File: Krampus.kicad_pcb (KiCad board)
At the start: 2 copper layers, 30 parts, among them J1 AVR-ISP-6, Q1 Q_NMOS_GSD, Q2 Q_NMOS_GSD, SW1 SW_SPDT_Flipped, SW2 SW_SPDT, U1 ATtiny4-TS-PROG

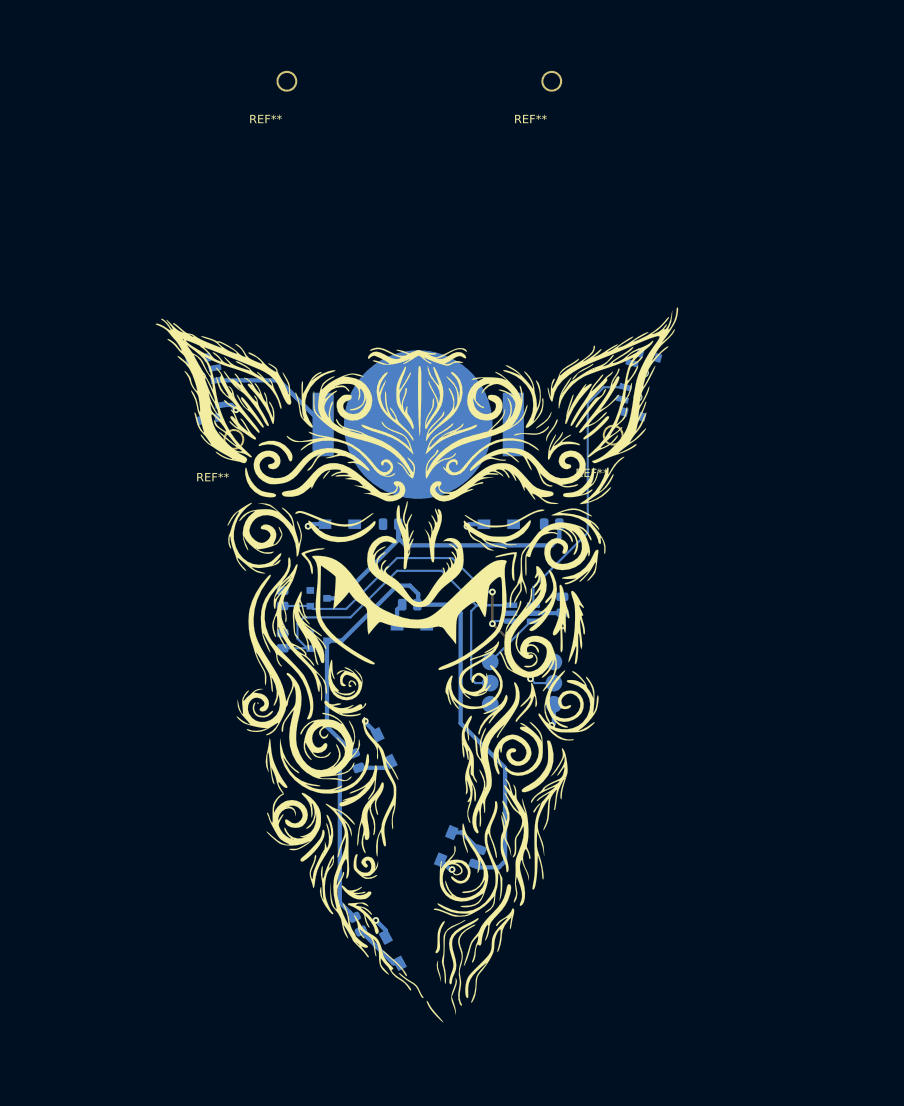
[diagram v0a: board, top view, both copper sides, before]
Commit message: Added copper pours and keepout areas for tongue and eyes. Everything done except edge cuts and revised mouth (want it to be gold)
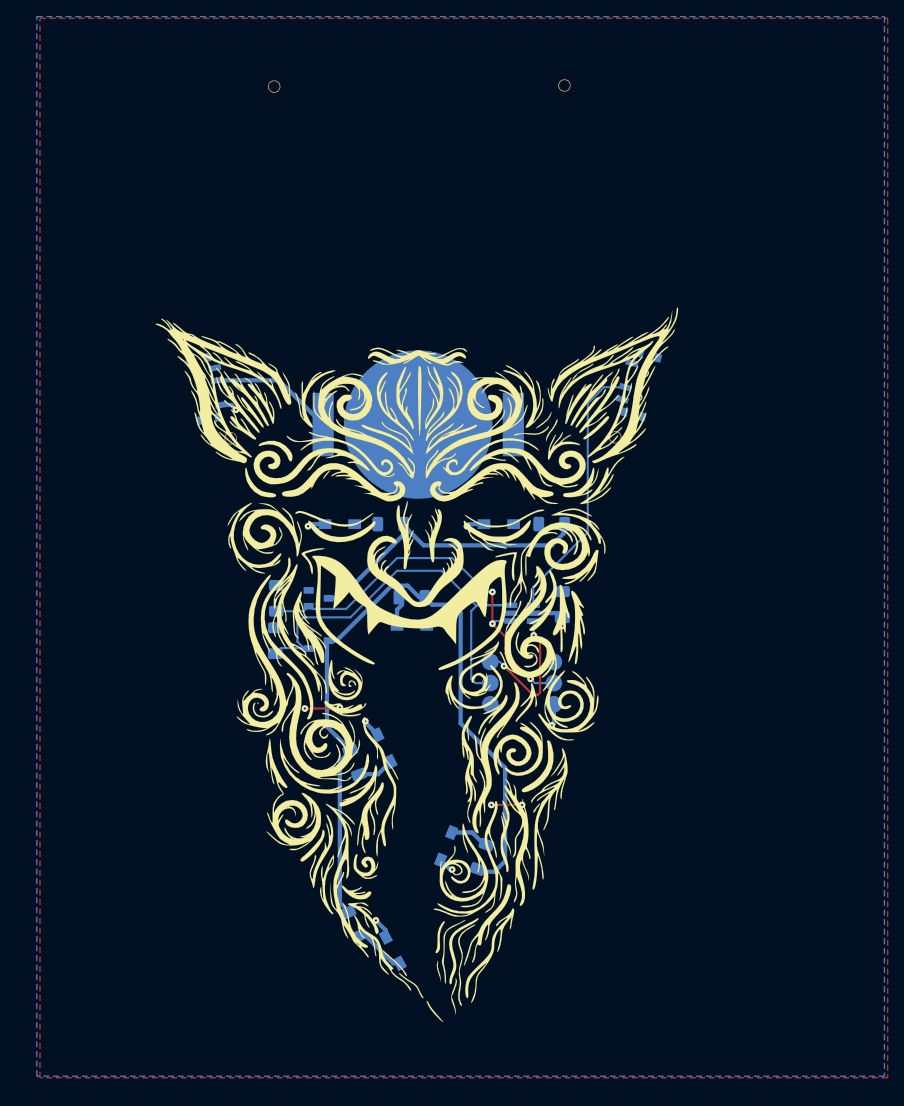
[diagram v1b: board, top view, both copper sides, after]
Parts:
- removed the REF** at (46.5, 80.8)
- removed the REF** at (91.9, 80.3)
- removed the REF** at (52.8, 37.8)
- removed the REF** at (84.6, 37.8)
- added G3: LOGO, Krampus:Red-back, F.Cu at (73.0, 89.5)
- added REF**: HOLE_WEARABLE_KRAMPUS, Krampus:HOLE_WEARABLE_KRAMPUS, F.Cu at (92.2, 80.5)
- added REF**: HOLE_WEARABLE_KRAMPUS, Krampus:HOLE_WEARABLE_KRAMPUS, F.Cu at (46.1, 80.6)
- added REF**: HOLE_WEARABLE_KRAMPUS, Krampus:HOLE_WEARABLE_KRAMPUS, F.Cu at (86.1, 38.4)
- added REF**: HOLE_WEARABLE_KRAMPUS, Krampus:HOLE_WEARABLE_KRAMPUS, F.Cu at (51.3, 38.5)
- C1: footprint Capacitor_SMD:C_0805_2012Metric -> Capacitor_SMD:C_1206_3216Metric_Pad1.33x1.80mm_HandSolder
- Q1, Q2: footprint Package_TO_SOT_SMD:SOT-23 -> Alpenglow:SOT-23-3
- R1, R2, R3, R4, R5, R6, R7, R8: footprint Resistor_SMD:R_0805_2012Metric -> Resistor_SMD:R_1206_3216Metric_Pad1.30x1.75mm_HandSolder
- moved R4 0.92 mm to (70.4, 95.6)
- moved R8 0.89 mm to (54.0, 100.8)
- moved R3 0.76 mm to (54.1, 95.8)
- moved R7 0.53 mm to (78.8, 126.7)
- moved R6 0.50 mm to (63.4, 134.8)
- moved R5 0.30 mm to (63.5, 115.4)
- moved G1 0.13 mm to (73.0, 89.4)
- renumbered G*** to G1, G*** to G2, G*** to G4, G*** to G5
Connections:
- SW1 pad : (no net) -> GND
- SW2 pad : (no net) -> GND
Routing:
- net /RESET: track 7.19 -> 16.9 mm, vias 0 -> 2
- net GND: track 0.00 -> 7.93 mm, vias 0 -> 4
- net /TONGUE: track 93.0 -> 90.9 mm
- net /EYES: track 36.7 -> 35.4 mm
- net /PB1: track 52.7 -> 54.0 mm
- net /PB0: track 47.2 -> 48.0 mm
- added copper zone on F.Cu, net +V
- added copper zone on B.Cu, net GND
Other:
- rule trace_min: 0.2 -> 0.1778
- rule via_min_size: 0.4 -> 0.254

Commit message: Added board outline, Changed teeth to gold, other tweaks and adjustments to layout
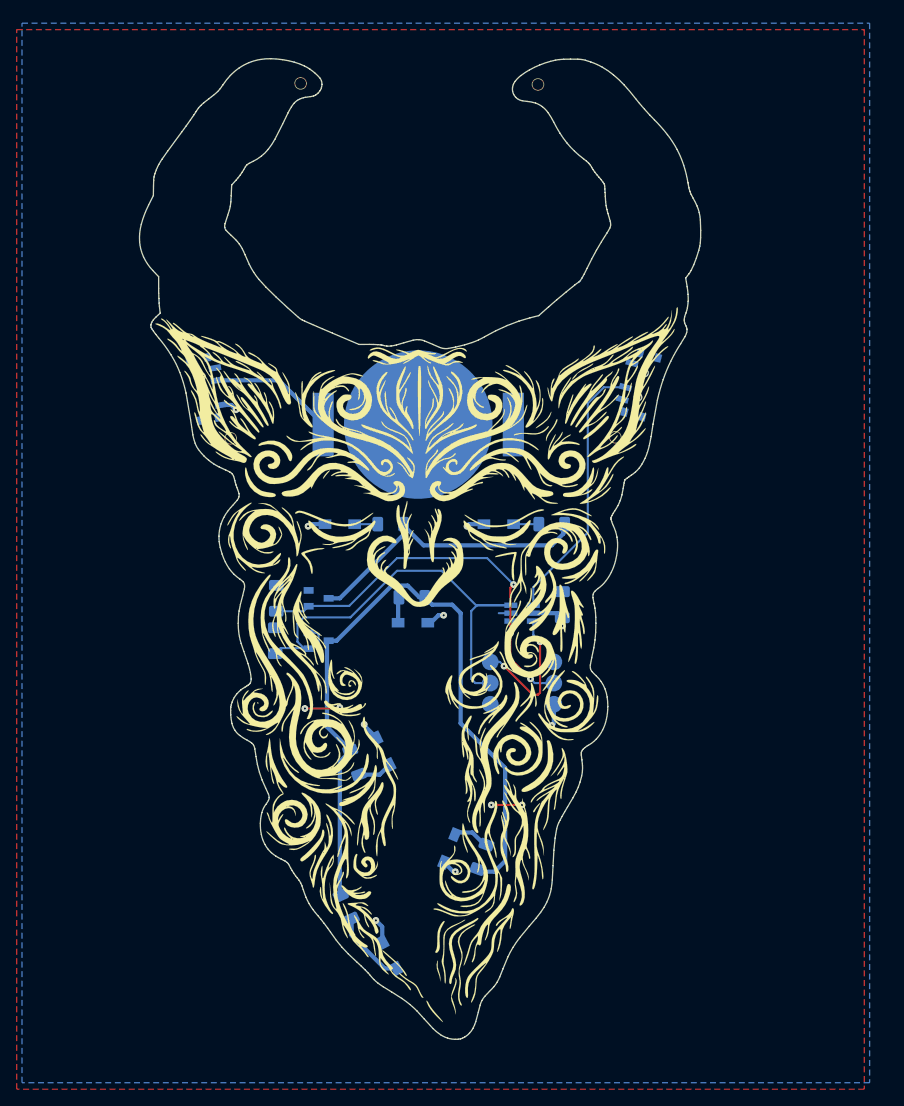
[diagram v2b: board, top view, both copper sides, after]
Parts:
- removed G1: LOGO, Krampus:Outline
- added G6: LOGO, Alpenglow:Alpenglow_Logo_Horiz_8mm, B.Cu at (98.2, 52.7)
- G4: footprint Krampus:White -> Krampus:WhitenoMouth
- G5: footprint Krampus:Gold -> Krampus:GoldwithTeeth
- moved G4 14.3 mm to (70.9, 103.6)
- moved REF** 3.20 mm to (54.5, 38.1)
- moved REF** 3.18 mm to (82.9, 38.2)
- moved R6 2.22 mm to (62.5, 132.8)
- moved D5 0.73 mm to (67.7, 138.6)
- moved D6 0.46 mm to (74.9, 125.7)
- moved D4 0.40 mm to (66.9, 114.1)
- moved D3 0.40 mm to (70.5, 98.7)
- moved G5 0.25 mm to (73.0, 89.8)
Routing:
- net GND: track 7.93 -> 12.8 mm
- net Net-(D2-Pad1): track 0.00 -> 3.02 mm
- net Net-(D5-Pad1): track 6.03 -> 9.01 mm
- net Net-(D1-Pad1): track 0.00 -> 2.77 mm
- net /TONGUE: track 90.9 -> 88.8 mm
- net /PB0: track 48.0 -> 49.2 mm
- net +V: track 22.3 -> 22.9 mm
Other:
- board outline added: 67.3 x 117.5 mm
- net class Default: via_drill 0.381 -> 0.254
- rule via_min_drill: 0.3 -> 0.254
- rule via_min_size: 0.254 -> 0.25146
- board text added: "@AlpenglowInd"
- board text added: "Merry Krampus!"
